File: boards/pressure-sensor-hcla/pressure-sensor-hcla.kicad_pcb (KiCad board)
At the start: 2 copper layers, 27.5 x 19 mm, 5 parts, among them J1 CONN_01X04, M3 MountingHole_3.2mm_M3, U1 HCLA-XXXX-DIP-X

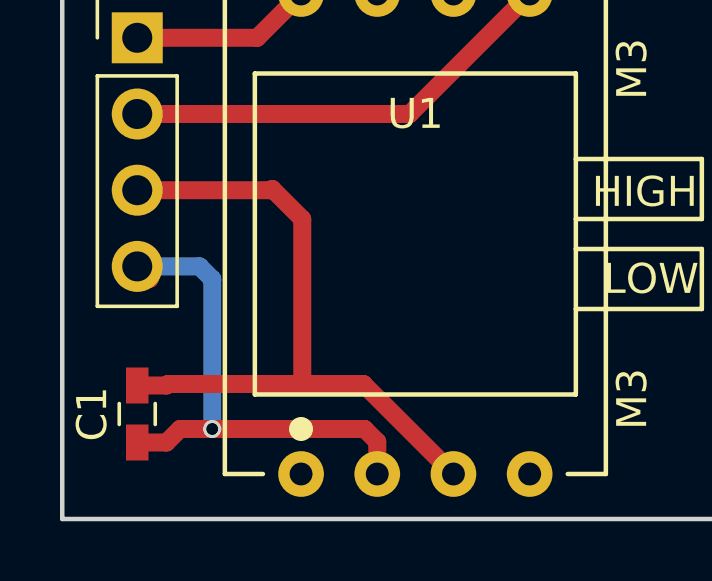
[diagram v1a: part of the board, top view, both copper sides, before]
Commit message: [pressure-sensor-hcla] Connect Vcc to +Vs Pin (not Vout)
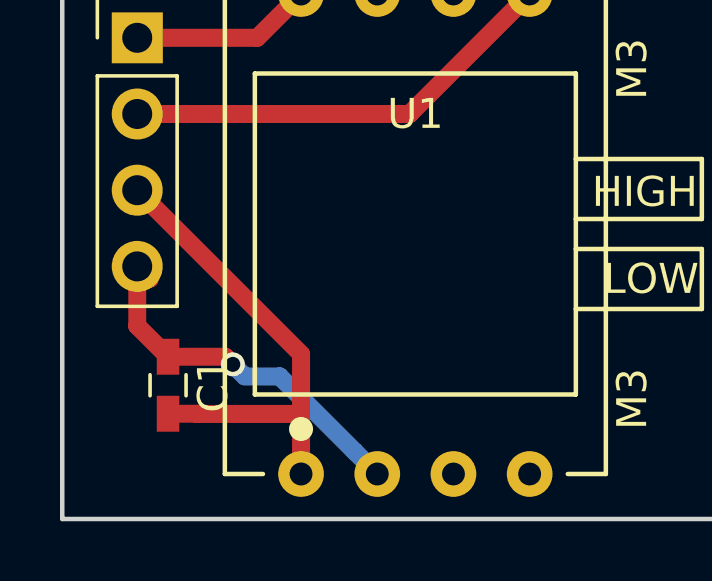
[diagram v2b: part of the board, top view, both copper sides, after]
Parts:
- moved C1 1.40 mm to (152.5, 102.0), turned to 90 degrees
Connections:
- U1 pad 1: Net-(U1-Pad1) -> /VCC
- U1 pad 3: /VCC -> (no net)
- U1 pad 4: Net-(U1-Pad4) -> (no net)
- U1 pad 6: Net-(U1-Pad6) -> (no net)
- U1 pad 7: Net-(U1-Pad7) -> (no net)
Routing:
- net /VCC: track 23.2 -> 16.2 mm
- net /GND: track 18.2 -> 12.6 mm
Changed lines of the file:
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@@
   (general
     (links 6)
-    (no_connects 0)
+    (no_connects 1)
     (area 148.924999 87.424999 176.575001 106.575001)
     (thickness 1.6)
     (drawings 9)
-    (tracks 25)
+    (tracks 20)
     (zones 0)
     (modules 5)
-    (nets 9)
+    (nets 5)
   )
   (page A4)
@@
     (via_min_size 0.4)
     (via_min_drill 0.3)
+    (user_via 0.8 0.5)
     (uvia_size 0.3)
     (uvia_drill 0.1)
@@
   (net 3 /SDA)
   (net 4 /SCL)
-  (net 5 "Net-(U1-Pad1)")
-  (net 6 "Net-(U1-Pad4)")
-  (net 7 "Net-(U1-Pad6)")
-  (net 8 "Net-(U1-Pad7)")
   (net_class Default "This is the default net class."
     (clearance 0.2)
@@
     (add_net /SDA)
     (add_net /VCC)
-    (add_net "Net-(U1-Pad1)")
-    (add_net "Net-(U1-Pad4)")
-    (add_net "Net-(U1-Pad6)")
-    (add_net "Net-(U1-Pad7)")
   )
   (module Capacitors_SMD:C_0603_HandSoldering (layer F.Cu)
-    (at 151.5 103 270)
+    (at 152.527 102.042 90)
     (descr "Capacitor SMD 0603, hand soldering")
     (tags "capacitor 0603")
     (attr smd)
-    (fp_text reference C1 (at 0 1.5 270) (layer F.SilkS)
-      (effects (font (size 1 1) (thickness 0.15)))
-    )
-    (fp_text value 100nF (at 0 3 270) (layer F.Fab)
-      (effects (font (size 1 1) (thickness 0.15)))
-    )
-    (fp_text user %R (at 0 -1.25 270) (layer F.Fab)
+    (fp_text reference C1 (at 0 1.5 90) (layer F.SilkS)
+      (effects (font (size 1 1) (thickness 0.15)))
+    )
+    (fp_text value 100nF (at 0 3 90) (layer F.Fab)
+      (effects (font (size 1 1) (thickness 0.15)))
+    )
+    (fp_text user %R (at 0 -1.25 90) (layer F.Fab)
       (effects (font (size 1 1) (thickness 0.15)))
     )
@@
     (fp_line (start 1.8 0.65) (end 1.8 -0.65) (layer F.CrtYd) (width 0.05))
     (fp_line (start 1.8 0.65) (end -1.8 0.65) (layer F.CrtYd) (width 0.05))
-    (pad 1 smd rect (at -0.95 0 270) (size 1.2 0.75) (layers F.Cu F.Paste F.Mask)
+    (pad 1 smd rect (at -0.95 0 90) (size 1.2 0.75) (layers F.Cu F.Paste F.Mask)
       (net 1 /VCC))
-    (pad 2 smd rect (at 0.95 0 270) (size 1.2 0.75) (layers F.Cu F.Paste F.Mask)
+    (pad 2 smd rect (at 0.95 0 90) (size 1.2 0.75) (layers F.Cu F.Paste F.Mask)
       (net 2 /GND))
     (model Capacitors_SMD.3dshapes/C_0603.wrl
@@
     (fp_line (start 12.7 0) (end 12.7 -16) (layer F.SilkS) (width 0.15))
     (pad 1 thru_hole circle (at 2.54 0) (size 1.524 1.524) (drill 0.762) (layers *.Cu *.Mask)
-      (net 5 "Net-(U1-Pad1)"))
+      (net 1 /VCC))
     (pad 2 thru_hole circle (at 5.08 0) (size 1.524 1.524) (drill 0.762) (layers *.Cu *.Mask)
       (net 2 /GND))
-    (pad 3 thru_hole circle (at 7.62 0) (size 1.524 1.524) (drill 0.762) (layers *.Cu *.Mask)
-      (net 1 /VCC))
-    (pad 4 thru_hole circle (at 10.16 0) (size 1.524 1.524) (drill 0.762) (layers *.Cu *.Mask)
-      (net 6 "Net-(U1-Pad4)"))
+    (pad 3 thru_hole circle (at 7.62 0) (size 1.524 1.524) (drill 0.762) (layers *.Cu *.Mask))
+    (pad 4 thru_hole circle (at 10.16 0) (size 1.524 1.524) (drill 0.762) (layers *.Cu *.Mask))
     (pad 5 thru_hole circle (at 10.16 -16) (size 1.524 1.524) (drill 0.762) (layers *.Cu *.Mask)
       (net 4 /SCL))
-    (pad 6 thru_hole circle (at 7.62 -16) (size 1.524 1.524) (drill 0.762) (layers *.Cu *.Mask)
-      (net 7 "Net-(U1-Pad6)"))
-    (pad 7 thru_hole circle (at 5.08 -16) (size 1.524 1.524) (drill 0.762) (layers *.Cu *.Mask)
-      (net 8 "Net-(U1-Pad7)"))
+    (pad 6 thru_hole circle (at 7.62 -16) (size 1.524 1.524) (drill 0.762) (layers *.Cu *.Mask))
+    (pad 7 thru_hole circle (at 5.08 -16) (size 1.524 1.524) (drill 0.762) (layers *.Cu *.Mask))
     (pad 8 thru_hole circle (at 2.54 -16) (size 1.524 1.524) (drill 0.762) (layers *.Cu *.Mask)
       (net 3 /SDA))
@@
     (pad 1 np_thru_hole circle (at 0 0) (size 3.2 3.2) (drill 3.2) (layers *.Cu *.Mask))
   )
+  (gr_text GND (at 155.5 98.5) (layer B.SilkS)
+    (effects (font (size 1.5 1.5) (thickness 0.3)) (justify mirror))
+  )
   (gr_text "rexus-viper\npressure-\nsensor-HCLA\n©rchojetzki" (at 163.5 97 90) (layer B.SilkS)
-    (effects (font (size 1.5 1.5) (thickness 0.3)) (justify mirror))
-  )
-  (gr_text GND (at 155.5 98.5) (layer B.SilkS)
     (effects (font (size 1.5 1.5) (thickness 0.3)) (justify mirror))
   )
@@
   (gr_line (start 149 87.5) (end 149 106.5) (layer Edge.Cuts) (width 0.15))
   (gr_line (start 176.5 87.5) (end 149 87.5) (layer Edge.Cuts) (width 0.15))
-  (segment (start 156 95.5) (end 155.96 95.54) (width 0.6) (layer F.Cu) (net 1))
-  (segment (start 155.96 95.54) (end 151.5 95.54) (width 0.6) (layer F.Cu) (net 1))
-  (segment (start 157 96.5) (end 156 95.5) (width 0.6) (layer F.Cu) (net 1))
-  (segment (start 157 102) (end 159.04 102) (width 0.6) (layer F.Cu) (net 1))
-  (segment (start 152.525 102) (end 157 102) (width 0.6) (layer F.Cu) (net 1))
-  (segment (start 157 102) (end 157 96.5) (width 0.6) (layer F.Cu) (net 1))
-  (segment (start 159.04 102) (end 162.04 105) (width 0.6) (layer F.Cu) (net 1))
-  (segment (start 151.5 102.05) (end 152.475 102.05) (width 0.6) (layer F.Cu) (net 1))
-  (segment (start 152.475 102.05) (end 152.525 102) (width 0.6) (layer F.Cu) (net 1))
-  (segment (start 154 98.5) (end 153.58 98.08) (width 0.6) (layer B.Cu) (net 2))
-  (segment (start 153.58 98.08) (end 151.5 98.08) (width 0.6) (layer B.Cu) (net 2))
+  (segment (start 156.96 101) (end 156.96 102.997) (width 0.6) (layer F.Cu) (net 1))
+  (segment (start 156.96 102.997) (end 156.96 105) (width 0.6) (layer F.Cu) (net 1))
+  (segment (start 152.527 102.992) (end 153.502 102.992) (width 0.6) (layer F.Cu) (net 1))
+  (segment (start 153.502 102.992) (end 153.507 102.997) (width 0.6) (layer F.Cu) (net 1))
+  (segment (start 153.507 102.997) (end 156.96 102.997) (width 0.6) (layer F.Cu) (net 1))
+  (segment (start 151.5 95.54) (end 156.96 101) (width 0.6) (layer F.Cu) (net 1))
+  (segment (start 154.686 101.346) (end 155.085999 101.745999) (width 0.6) (layer B.Cu) (net 2))
+  (segment (start 155.085999 101.745999) (end 156.245999 101.745999) (width 0.6) (layer B.Cu) (net 2))
+  (segment (start 156.245999 101.745999) (end 158.738001 104.238001) (width 0.6) (layer B.Cu) (net 2))
+  (segment (start 158.738001 104.238001) (end 159.5 105) (width 0.6) (layer B.Cu) (net 2))
+  (segment (start 152.527 101.092) (end 154.432 101.092) (width 0.6) (layer F.Cu) (net 2))
+  (segment (start 154.432 101.092) (end 154.686 101.346) (width 0.6) (layer F.Cu) (net 2))
+  (via (at 154.686 101.346) (size 0.8) (drill 0.5) (layers F.Cu B.Cu) (net 2))
+  (segment (start 151.5 98.08) (end 151.5 100.065) (width 0.6) (layer F.Cu) (net 2))
+  (segment (start 151.5 100.065) (end 152.527 101.092) (width 0.6) (layer F.Cu) (net 2))
   (segment (start 151.92 98.5) (end 151.5 98.08) (width 0.6) (layer F.Cu) (net 2))
-  (segment (start 154 103.5) (end 154 98.5) (width 0.6) (layer B.Cu) (net 2))
-  (segment (start 154.5 103.5) (end 152.925 103.5) (width 0.6) (layer F.Cu) (net 2))
-  (segment (start 159.07763 103.5) (end 154.5 103.5) (width 0.6) (layer F.Cu) (net 2))
-  (segment (start 154.5 103.5) (end 154 103.5) (width 0.6) (layer F.Cu) (net 2))
-  (via (at 154 103.5) (size 0.6) (drill 0.4) (layers F.Cu B.Cu) (net 2))
-  (segment (start 152.925 103.5) (end 152.475 103.95) (width 0.6) (layer F.Cu) (net 2))
-  (segment (start 152.475 103.95) (end 151.5 103.95) (width 0.6) (layer F.Cu) (net 2))
-  (segment (start 159.5 105) (end 159.5 103.92237) (width 0.6) (layer F.Cu) (net 2))
-  (segment (start 159.5 103.92237) (end 159.07763 103.5) (width 0.6) (layer F.Cu) (net 2))
   (segment (start 151.5 90.46) (end 155.5 90.46) (width 0.6) (layer F.Cu) (net 3))
   (segment (start 155.5 90.46) (end 156.96 89) (width 0.6) (layer F.Cu) (net 3))

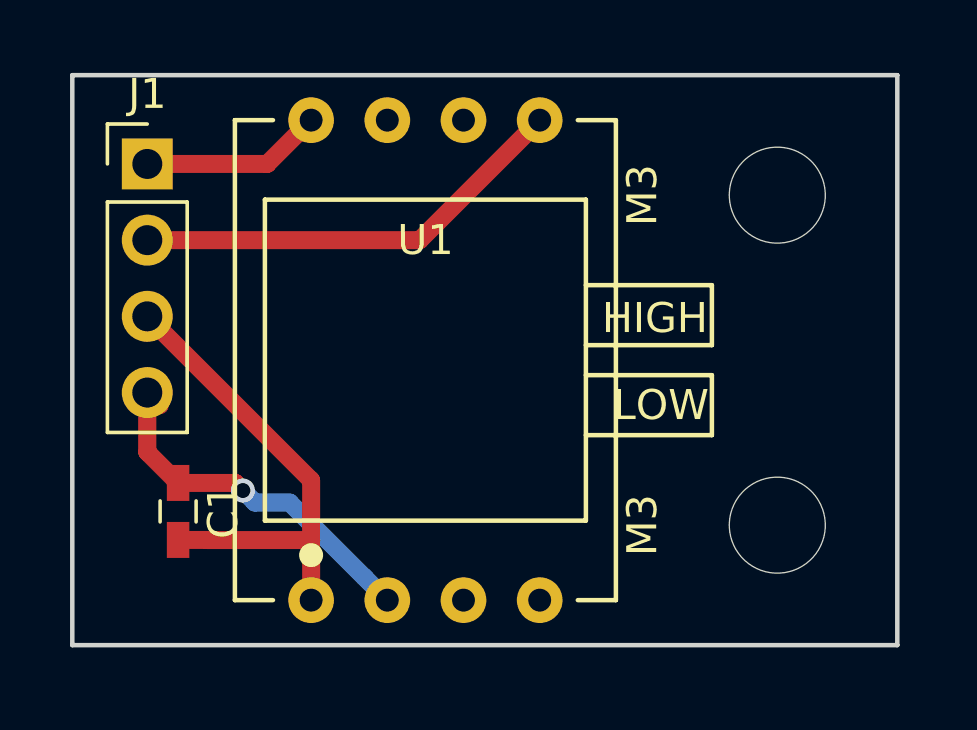
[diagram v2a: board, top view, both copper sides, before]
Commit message: [pressure-sensor-hcla] add GND plane
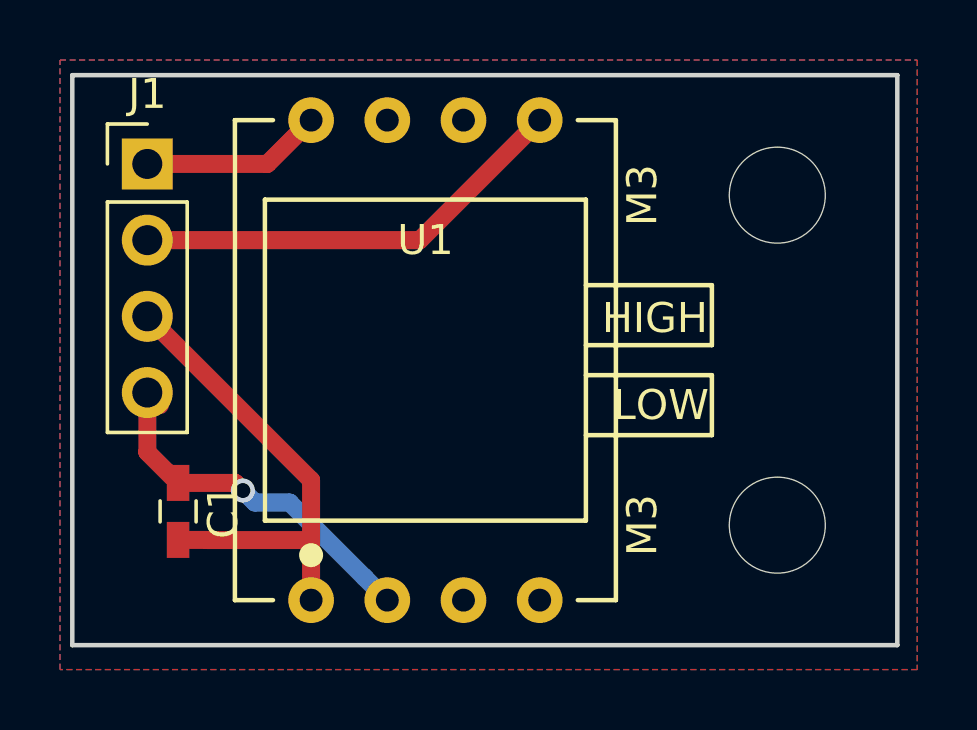
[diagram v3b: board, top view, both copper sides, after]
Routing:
- added copper zone on B.Cu, net /GND
- added copper zone on F.Cu, net /GND
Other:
- rule pad_to_mask_clearance: 0.2 -> 0.1
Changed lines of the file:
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@@
     (links 6)
     (no_connects 1)
-    (area 148.924999 87.424999 176.575001 106.575001)
+    (area 147.025 85.525 182.057143 109.075)
     (thickness 1.6)
     (drawings 9)
@@
     (last_trace_width 0.6)
     (trace_clearance 0.2)
-    (zone_clearance 0.508)
+    (zone_clearance 0.3)
     (zone_45_only yes)
     (trace_min 0.2)
@@
     (pad_size 1.524 1.524)
     (pad_drill 0.762)
-    (pad_to_mask_clearance 0.2)
+    (pad_to_mask_clearance 0.1)
     (aux_axis_origin 0 0)
     (visible_elements 7FFFFFFF)
@@
     (min_thickness 0.254)
     (keepout (tracks not_allowed) (vias not_allowed) (copperpour not_allowed))
-    (fill (arc_segments 16) (thermal_gap 0.508) (thermal_bridge_width 0.508))
+    (fill yes (arc_segments 16) (thermal_gap 0.508) (thermal_bridge_width 0.508))
     (polygon
       (pts
@@
     (min_thickness 0.254)
     (keepout (tracks not_allowed) (vias not_allowed) (copperpour not_allowed))
-    (fill (arc_segments 16) (thermal_gap 0.508) (thermal_bridge_width 0.508))
+    (fill yes (arc_segments 16) (thermal_gap 0.508) (thermal_bridge_width 0.508))
     (polygon
       (pts
@@
     (min_thickness 0.254)
     (keepout (tracks not_allowed) (vias not_allowed) (copperpour not_allowed))
-    (fill (arc_segments 16) (thermal_gap 0.508) (thermal_bridge_width 0.508))
+    (fill yes (arc_segments 16) (thermal_gap 0.508) (thermal_bridge_width 0.508))
     (polygon
       (pts
@@
     (min_thickness 0.254)
     (keepout (tracks not_allowed) (vias not_allowed) (copperpour not_allowed))
-    (fill (arc_segments 16) (thermal_gap 0.508) (thermal_bridge_width 0.508))
+    (fill yes (arc_segments 16) (thermal_gap 0.508) (thermal_bridge_width 0.508))
     (polygon
       (pts
@@
       )
     )
+  )
+  (zone (net 2) (net_name /GND) (layer F.Cu) (hatch edge 0.508)
+    (connect_pads (clearance 0.3))
+    (min_thickness 0.25)
+    (fill yes (arc_segments 16) (thermal_gap 0.3) (thermal_bridge_width 0.3))
+    (polygon
+      (pts
+        (xy 148.59 86.995) (xy 177.165 86.995) (xy 177.165 107.315) (xy 148.59 107.315)
+      )
+    )
+  )
+  (zone (net 2) (net_name /GND) (layer B.Cu) (hatch edge 0.508)
+    (connect_pads (clearance 0.3))
+    (min_thickness 0.25)
+    (fill yes (arc_segments 16) (thermal_gap 0.3) (thermal_bridge_width 0.3))
+    (polygon
+      (pts
+        (xy 148.59 86.995) (xy 177.165 86.995) (xy 177.165 107.315) (xy 148.59 107.315)
+      )
+    )
